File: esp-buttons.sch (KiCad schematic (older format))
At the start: 41 parts, among them CON1 POWER_5V, P1 CONN_BUTTON1, P2 CONN_BUTTON2, P3 CONN_BUTTON3, P4 CONN_BUTTON4, P5 CONN_BUTTON5, P6 UART_DEBUG, P7 UART, Q1 IRLML2502TRPBF, Q2 IRLML2502TRPBF, Q3 IRLML2502TRPBF, Q4 IRLML2502TRPBF, Q5 IRLML2502TRPBF, SW1 RESET_BUTTON, SW2 PROG_BUTTON, U1 ESP-07v2, U2 LD1117S33CTR, U3 FT230XS

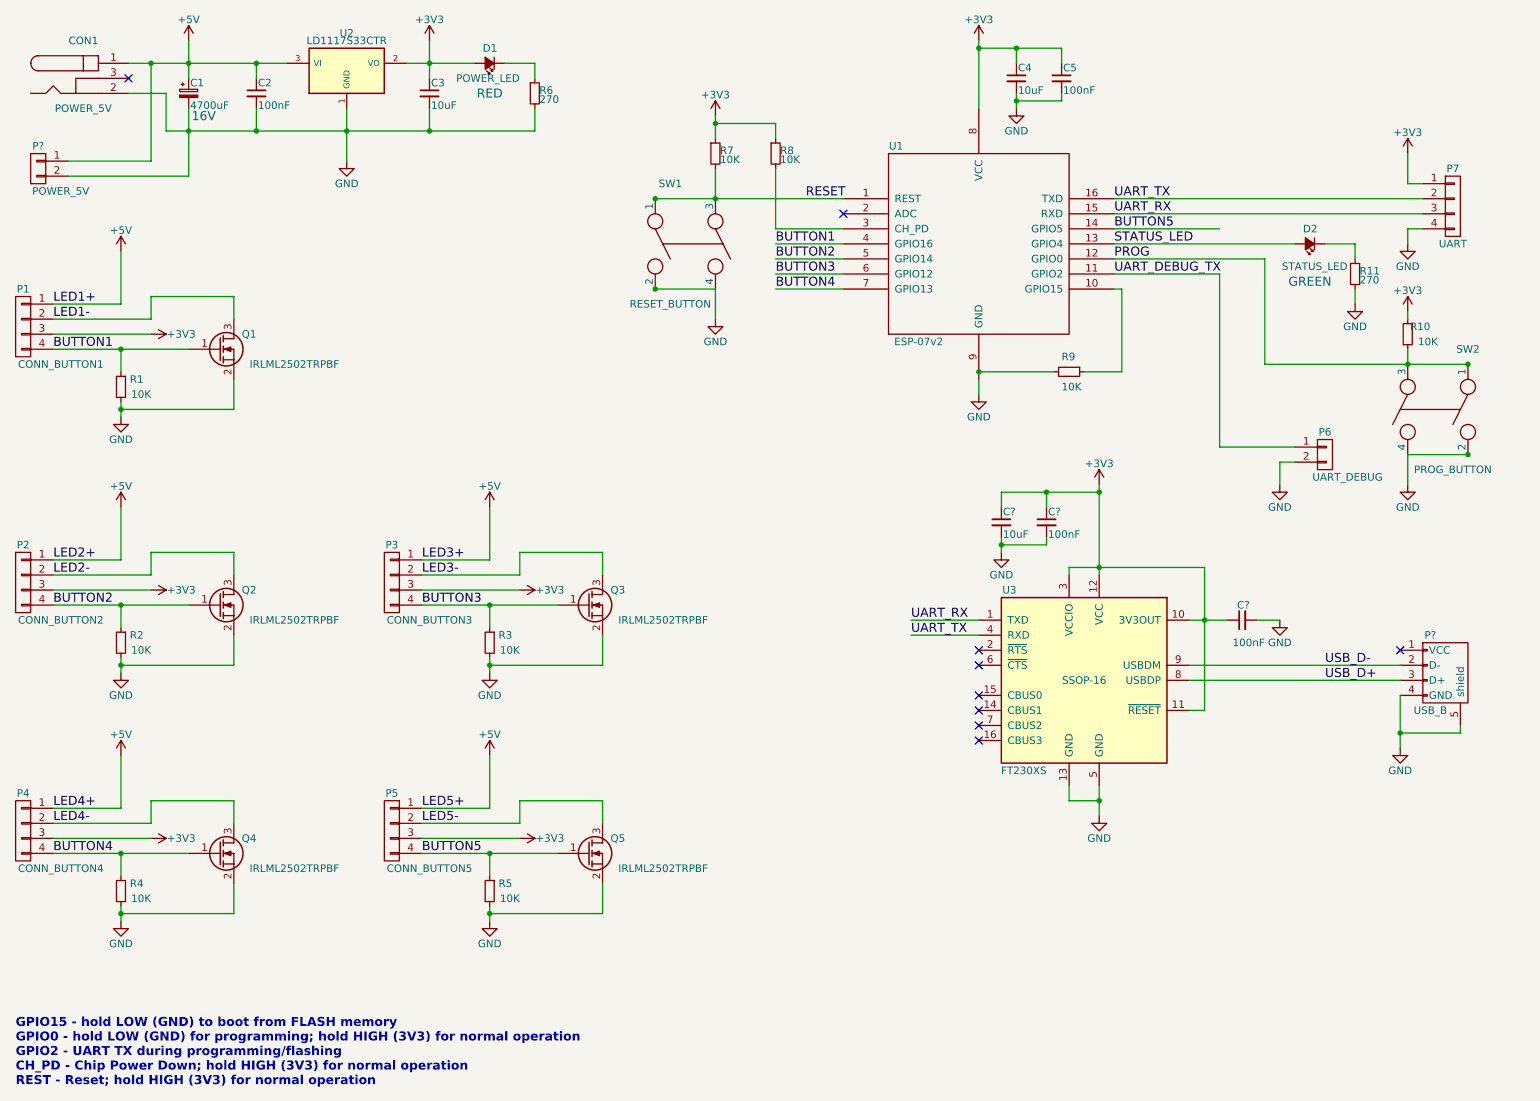
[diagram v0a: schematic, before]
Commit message: Annotated the rest of the schematic
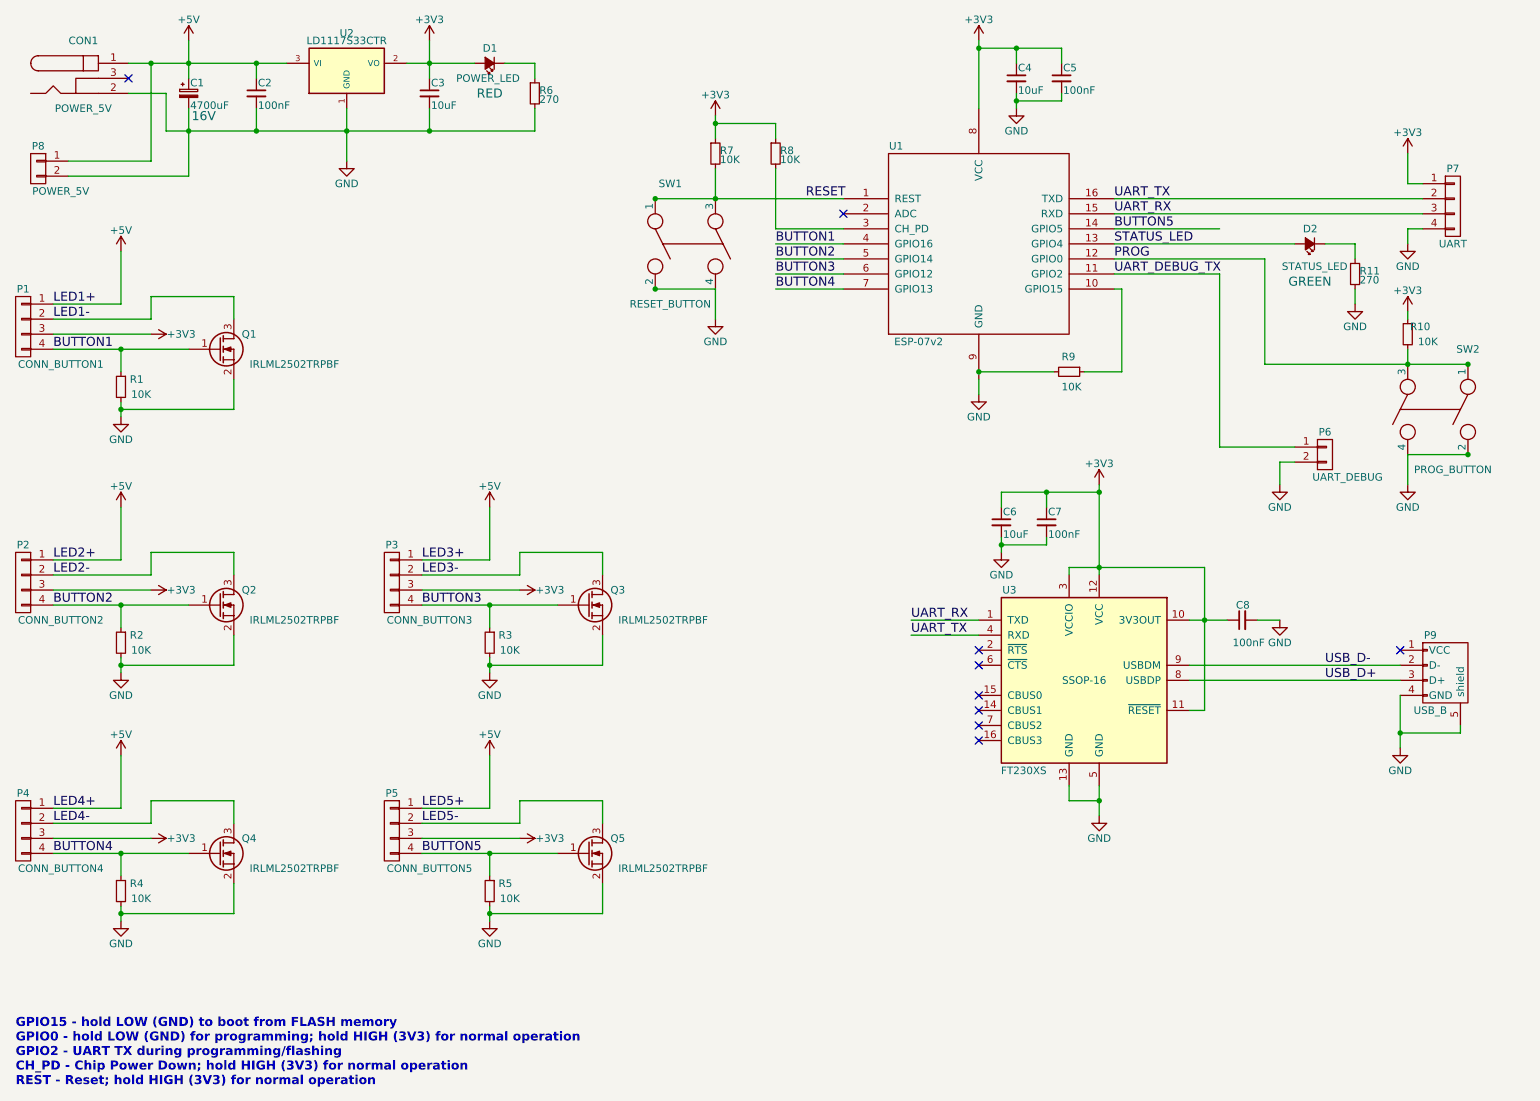
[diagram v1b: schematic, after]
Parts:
- gave numbers to parts that had none: 5
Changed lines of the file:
@@
 $EndComp
 $Comp
-L GND #PWR23
+L GND #PWR24
 U 1 1 57C6B359
 P 7200 1250
-F 0 "#PWR23" H 7200 1000 50  0001 C CNN
+F 0 "#PWR24" H 7200 1000 50  0001 C CNN
 F 1 "GND" H 7200 1100 50  0000 C CNN
 F 2 "" H 7200 1250 50  0000 C CNN
@@
 $EndComp
 $Comp
-L GND #PWR25
+L GND #PWR29
 U 1 1 57C70472
 P 9450 2550
-F 0 "#PWR25" H 9450 2300 50  0001 C CNN
+F 0 "#PWR29" H 9450 2300 50  0001 C CNN
 F 1 "GND" H 9450 2400 50  0000 C CNN
 F 2 "" H 9450 2550 50  0000 C CNN
@@
 $EndComp
 $Comp
-L GND #PWR27
+L GND #PWR32
 U 1 1 57C82907
 P 9800 2150
-F 0 "#PWR27" H 9800 1900 50  0001 C CNN
+F 0 "#PWR32" H 9800 1900 50  0001 C CNN
 F 1 "GND" H 9800 2000 50  0000 C CNN
 F 2 "" H 9800 2150 50  0000 C CNN
@@
 $EndComp
 $Comp
-L +3V3 #PWR26
+L +3V3 #PWR31
 U 1 1 57C82955
 P 9800 1550
-F 0 "#PWR26" H 9800 1400 50  0001 C CNN
+F 0 "#PWR31" H 9800 1400 50  0001 C CNN
 F 1 "+3V3" H 9800 1690 50  0000 C CNN
 F 2 "" H 9800 1550 50  0000 C CNN
@@
 $EndComp
 $Comp
-L +3V3 #PWR28
+L +3V3 #PWR33
 U 1 1 57C83F12
 P 9800 2600
-F 0 "#PWR28" H 9800 2450 50  0001 C CNN
+F 0 "#PWR33" H 9800 2450 50  0001 C CNN
 F 1 "+3V3" H 9800 2740 50  0000 C CNN
 F 2 "" H 9800 2600 50  0000 C CNN
@@
 $EndComp
 $Comp
-L GND #PWR29
+L GND #PWR34
 U 1 1 57C83F22
 P 9800 3750
-F 0 "#PWR29" H 9800 3500 50  0001 C CNN
+F 0 "#PWR34" H 9800 3500 50  0001 C CNN
 F 1 "GND" H 9800 3600 50  0000 C CNN
 F 2 "" H 9800 3750 50  0000 C CNN
@@
 BUTTON4
 $Comp
-L GND #PWR24
+L GND #PWR27
 U 1 1 57C97F98
 P 8950 3750
-F 0 "#PWR24" H 8950 3500 50  0001 C CNN
+F 0 "#PWR27" H 8950 3500 50  0001 C CNN
 F 1 "GND" H 8950 3600 50  0000 C CNN
 F 2 "" H 8950 3750 50  0000 C CNN
@@
 NoConn ~ 6950 4950
 $Comp
-L USB_B P?
+L USB_B P9
 U 1 1 57E776BA
 P 10050 5050
-F 0 "P?" V 9750 4950 50  0000 C CNN
+F 0 "P9" V 9750 4950 50  0000 C CNN
 F 1 "USB_B" V 10250 4950 50  0000 C CNN
 F 2 "Connect:USB_B" V 10000 4950 50  0001 C CNN
@@
 NoConn ~ 9750 4850
 $Comp
-L GND #PWR?
+L GND #PWR26
 U 1 1 57E77E29
 P 7750 5950
-F 0 "#PWR?" H 7750 5700 50  0001 C CNN
+F 0 "#PWR26" H 7750 5700 50  0001 C CNN
 F 1 "GND" H 7750 5800 50  0000 C CNN
 F 2 "" H 7750 5950 50  0000 C CNN
@@
 $EndComp
 $Comp
-L GND #PWR?
+L GND #PWR30
 U 1 1 57E7865B
 P 9750 5500
-F 0 "#PWR?" H 9750 5250 50  0001 C CNN
+F 0 "#PWR30" H 9750 5250 50  0001 C CNN
 F 1 "GND" H 9750 5350 50  0000 C CNN
 F 2 "" H 9750 5500 50  0000 C CNN
@@
 USB_D+
 $Comp
-L +3V3 #PWR?
+L +3V3 #PWR25
 U 1 1 57E78DE0
 P 7750 3750
-F 0 "#PWR?" H 7750 3600 50  0001 C CNN
+F 0 "#PWR25" H 7750 3600 50  0001 C CNN
 F 1 "+3V3" H 7750 3890 50  0000 C CNN
 F 2 "" H 7750 3750 50  0000 C CNN
@@
 UART_RX
 $Comp
-L CONN_01X02 P?
+L CONN_01X02 P8
 U 1 1 57E79EDB
 P 700 1650
-F 0 "P?" H 700 1800 50  0000 C CNN
+F 0 "P8" H 700 1800 50  0000 C CNN
 F 1 "POWER_5V" H 550 1500 50  0000 C CNN
 F 2 "Terminal_Blocks:TerminalBlock_Pheonix_PT-3.5mm_2pol" H 700 1650 50  0001 C CNN
@@
 NoConn ~ 1300 1050
 $Comp
-L C_Small C?
+L C_Small C6
 U 1 1 57E7B15D
 P 7100 4000
-F 0 "C?" H 7110 4070 50  0000 L CNN
+F 0 "C6" H 7110 4070 50  0000 L CNN
 F 1 "10uF" H 7110 3920 50  0000 L CNN
 F 2 "Capacitors_SMD:C_1210_HandSoldering" H 7100 4000 50  0001 C CNN
@@
 $EndComp
 $Comp
-L C_Small C?
+L C_Small C7
 U 1 1 57E7B163
 P 7400 4000
-F 0 "C?" H 7410 4070 50  0000 L CNN
+F 0 "C7" H 7410 4070 50  0000 L CNN
 F 1 "100nF" H 7410 3920 50  0000 L CNN
 F 2 "Capacitors_SMD:C_1206_HandSoldering" H 7400 4000 50  0001 C CNN
@@
 $EndComp
 $Comp
-L C_Small C?
+L C_Small C8
 U 1 1 57E7B263
 P 8700 4650
-F 0 "C?" V 8800 4600 50  0000 L CNN
+F 0 "C8" V 8800 4600 50  0000 L CNN
 F 1 "100nF" V 8550 4500 50  0000 L CNN
 F 2 "Capacitors_SMD:C_1206_HandSoldering" H 8700 4650 50  0001 C CNN
@@
 $EndComp
 $Comp
-L GND #PWR?
+L GND #PWR28
 U 1 1 57E7B4D1
 P 8950 4650
-F 0 "#PWR?" H 8950 4400 50  0001 C CNN
+F 0 "#PWR28" H 8950 4400 50  0001 C CNN
 F 1 "GND" H 8950 4500 50  0000 C CNN
 F 2 "" H 8950 4650 50  0000 C CNN
@@
 	7100 4150 7100 4200
 $Comp
-L GND #PWR?
+L GND #PWR23
 U 1 1 57E7C5E9
 P 7100 4200
-F 0 "#PWR?" H 7100 3950 50  0001 C CNN
+F 0 "#PWR23" H 7100 3950 50  0001 C CNN
 F 1 "GND" H 7100 4050 50  0000 C CNN
 F 2 "" H 7100 4200 50  0000 C CNN

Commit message: Fixed the footprint for the SW1 button
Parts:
- SW1: footprint Buttons_Switches_SMD:SW_SPST_EVPBF -> Buttons_Switches_ThroughHole:SW_PUSH_6mm
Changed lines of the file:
@@
 F 0 "SW1" V 4600 2050 50  0000 C CNN
 F 1 "RESET_BUTTON" V 5400 2050 50  0000 C CNN
-F 2 "Buttons_Switches_SMD:SW_SPST_EVPBF" H 5000 2150 50  0001 C CNN
+F 2 "Buttons_Switches_ThroughHole:SW_PUSH_6mm" H 5000 2150 50  0001 C CNN
 F 3 "" H 5000 2150 50  0000 C CNN
 	1    5000 2150

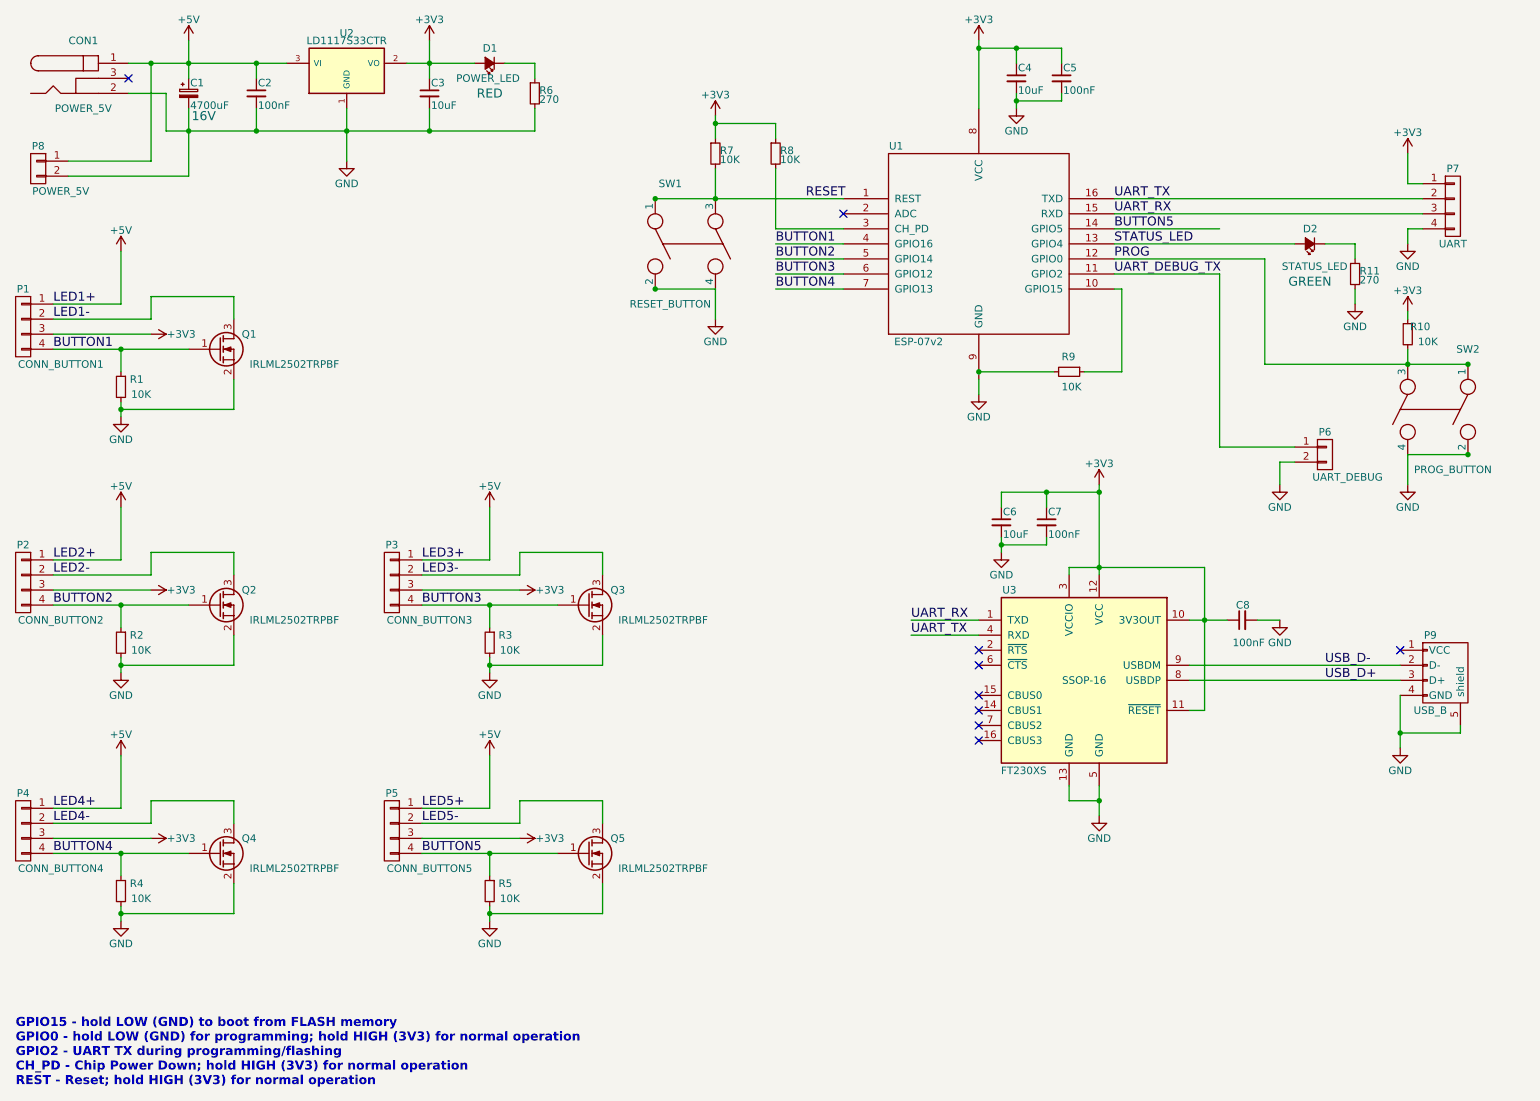
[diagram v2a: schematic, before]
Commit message: Fixing most of the  ERC errors (I guess)
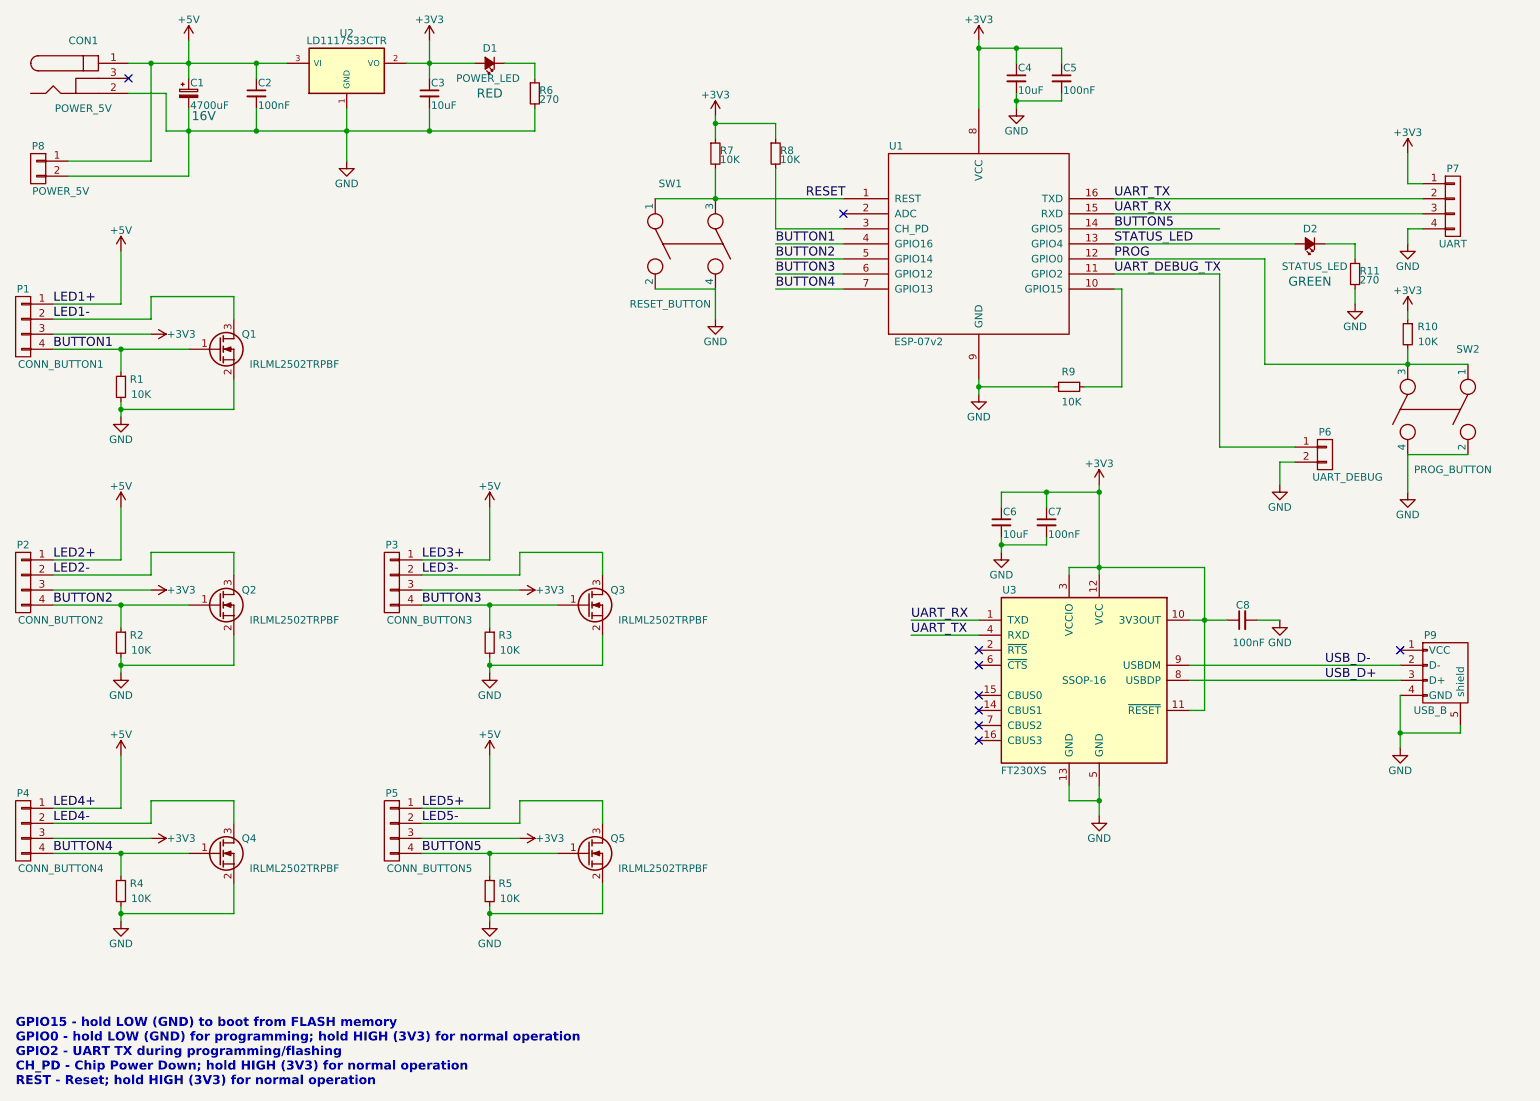
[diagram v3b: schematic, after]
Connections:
- net GND: now also R9.2
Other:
- moved on the sheet: R9

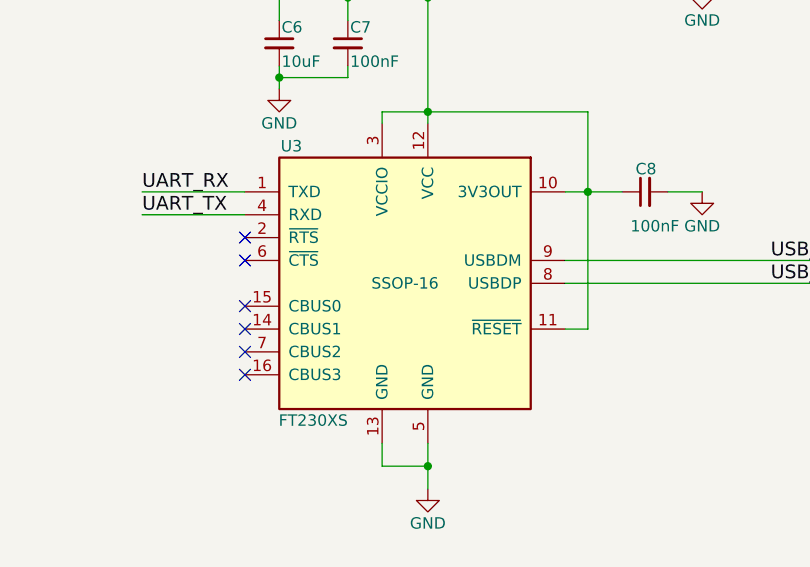
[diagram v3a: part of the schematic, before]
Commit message: Assigning footprints to sch symbols for the ESP-07 & FT230XS
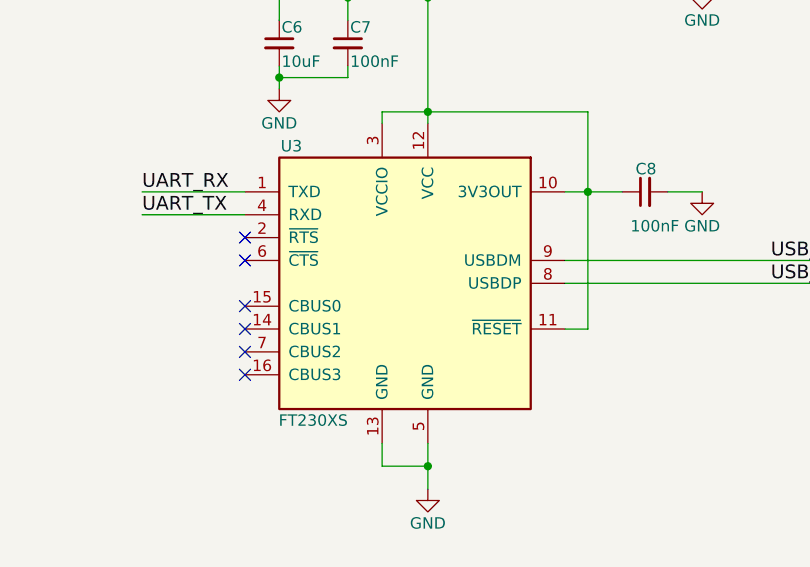
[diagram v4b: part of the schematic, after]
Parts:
- U1: footprint (none) -> ESP8266:ESP-07v2
- U3: footprint SSOP-16 -> Housings_SSOP:SSOP-16_3.9x4.9mm_Pitch0.635mm
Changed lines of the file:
@@
 F 0 "U1" H 6400 2800 50  0000 C CNN
 F 1 "ESP-07v2" H 6550 1500 50  0000 C CNN
-F 2 "" H 6950 2150 50  0001 C CNN
+F 2 "ESP8266:ESP-07v2" H 6950 2150 50  0001 C CNN
 F 3 "" H 6950 2150 50  0001 C CNN
 	1    6950 2150
@@
 F 0 "U3" H 8100 5650 50  0000 L CNN
 F 1 "FT230XS" H 7900 4450 50  0000 L CNN
-F 2 "SSOP-16" H 7650 5050 50  0000 C CNN
+F 2 "Housings_SSOP:SSOP-16_3.9x4.9mm_Pitch0.635mm" H 7650 5050 50  0001 C CNN
 F 3 "" H 7650 5050 50  0000 C CNN
 	1    7650 5050
